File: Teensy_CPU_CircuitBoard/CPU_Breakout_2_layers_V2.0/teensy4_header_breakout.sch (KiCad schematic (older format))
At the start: 0 parts

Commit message: Start of V3 STM32
Imported symbols/footprints ...
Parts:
- added D9: D_RPP_Input_PMEG4010EGWX, Teensy_Footprint_Library:D_RPP_PMEG4010EGWX, symbol teensy4_header_breakout-cache:D_RPP_Input_PMEG4010EGWX
- added PS1: TEL_5-1211, Teensy_Footprint_Library:TEL51211, symbol teensy4_header_breakout-cache:TEL_5-1211
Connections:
- new net: PS1.2 (-VIN_(GND)_1), PS1.3 (-VIN_(GND)_2)
- new net: D9.1 (K), PS1.22 (+VIN_(VCC)_1), PS1.23 (+VIN_(VCC)_2)
- new net 12V_IN: D9.2 (A)
- new net Ground: PS1.16 (-VOUT)
- new net Vinn_5V: PS1.14 (+VOUT)
- no-connect marks 0 -> 1
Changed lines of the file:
@@
 $Descr A4 11693 8268
 encoding utf-8
-Sheet 1 6
+Sheet 1 5
 Title ""
 Date ""
@@
 $EndDescr
 $Sheet
-S 2400 4200 950  1150
+S 1650 4650 950  1150
 U 5DE81E30
 F0 "LM324" 50
@@
 $EndSheet
 $Sheet
-S 2300 1200 1200 1200
+S 1500 1150 1200 1200
 U 5DE8C472
 F0 "MCP2551" 50
@@
 $EndSheet
 $Sheet
-S 4500 1000 1100 1600
+S 3700 950  1100 1600
 U 5DE8C4DF
 F0 "microSD" 50
@@
 $EndSheet
 $Sheet
-S 6650 950  1000 1750
-U 5DE8C550
-F0 "VoltageReg" 50
-F1 "NCV890430MW50TXG.sch" 50
-$EndSheet
-$Sheet
-S 6700 3650 1050 1900
+S 3750 4200 1050 1900
 U 5DE8C5CE
 F0 "T4" 50
 F1 "Teensy4.0.sch" 50
 $EndSheet
+Text GLabel 9550 1650 2    50   Input ~ 0
+12V_IN
+Text GLabel 9250 1950 2    50   Input ~ 0
+Vinn_5V
+Text GLabel 6700 1650 0    50   Input ~ 0
+12V_Ground
+$Comp
+L teensy4_header_breakout-cache:TEL_5-1211 PS1
+U 1 1 5FAC174D
+P 7350 1650
+F 0 "PS1" H 8300 1915 50  0000 C CNN
+F 1 "TEL_5-1211" H 8300 1824 50  0000 C CNN
+F 2 "Teensy_Footprint_Library:TEL51211" H 9100 1750 50  0001 L CNN
+F 3 "https://www.tracopower.com/products/tel5.pdf" H 9100 1650 50  0001 L CNN
+F 4 "TEL5 DC-DC converter,9-18Vin 5V 5W TRACOPOWER Isolated DC-DC Converter, Vin 9  18 V dc, Vout 5V dc, I/O isolation 1500V dc" H 9100 1550 50  0001 L CNN "Description"
+F 5 "10.45" H 9100 1450 50  0001 L CNN "Height"
+F 6 "Traco Power" H 9100 1350 50  0001 L CNN "Manufacturer_Name"
+F 7 "TEL 5-1211" H 9100 1250 50  0001 L CNN "Manufacturer_Part_Number"
+F 8 "495-TEL-5-1211" H 9100 950 50  0001 L CNN "Mouser Part Number"
+F 9 "https://www.mouser.co.uk/ProductDetail/TRACO-Power/TEL-5-1211?qs=ckJk83FOD0WBOuRLitdGqQ%3D%3D" H 9100 850 50  0001 L CNN "Mouser Price/Stock"
+	1    7350 1650
+	1    0    0    -1
+$EndComp
+NoConn ~ 7350 1850
+Text GLabel 9250 1850 2    50   Input ~ 0
+Ground
+Wire Wire Line
+	9250 1750 9250 1650
+Wire Wire Line
+	7350 1650 7350 1750
+$Comp
+L teensy4_header_breakout-cache:D_RPP_Input_PMEG4010EGWX D9
+U 1 1 5FACD4C4
+P 9400 1650
+F 0 "D9" H 9400 1867 50  0000 C CNN
+F 1 "D_RPP_Input_PMEG4010EGWX" H 9400 1776 50  0000 C CNN
+F 2 "Teensy_Footprint_Library:D_RPP_PMEG4010EGWX" H 9400 1650 50  0001 C CNN
+F 3 "~" H 9400 1650 50  0001 C CNN
+	1    9400 1650
+	1    0    0    -1
+$EndComp
+Connection ~ 9250 1650
 $EndSCHEMATC

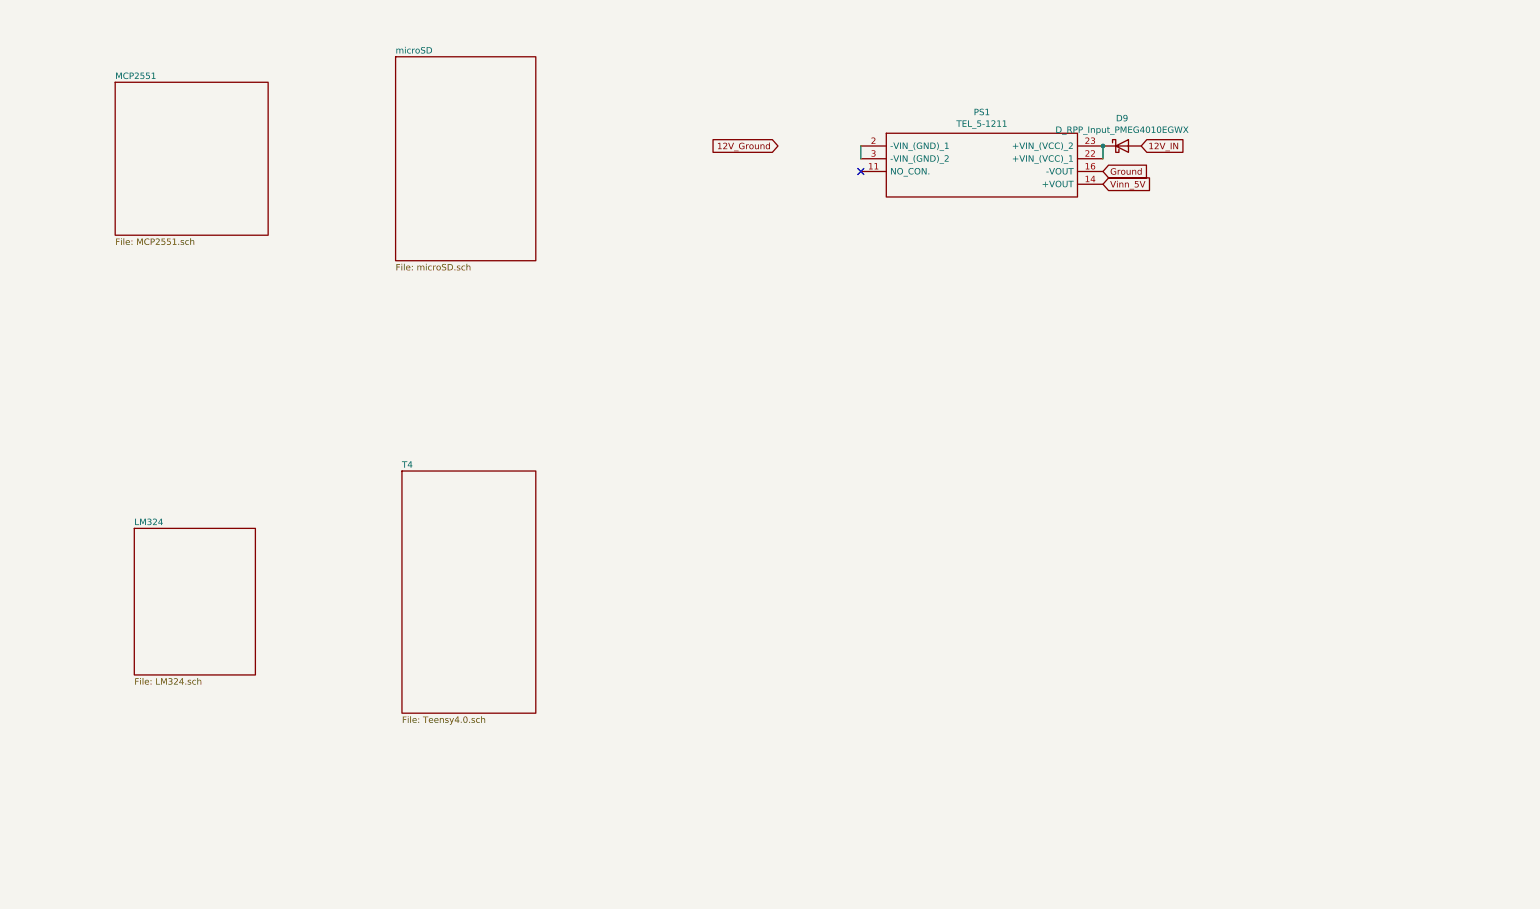
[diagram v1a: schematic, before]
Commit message: Suspension disp senson schematic done
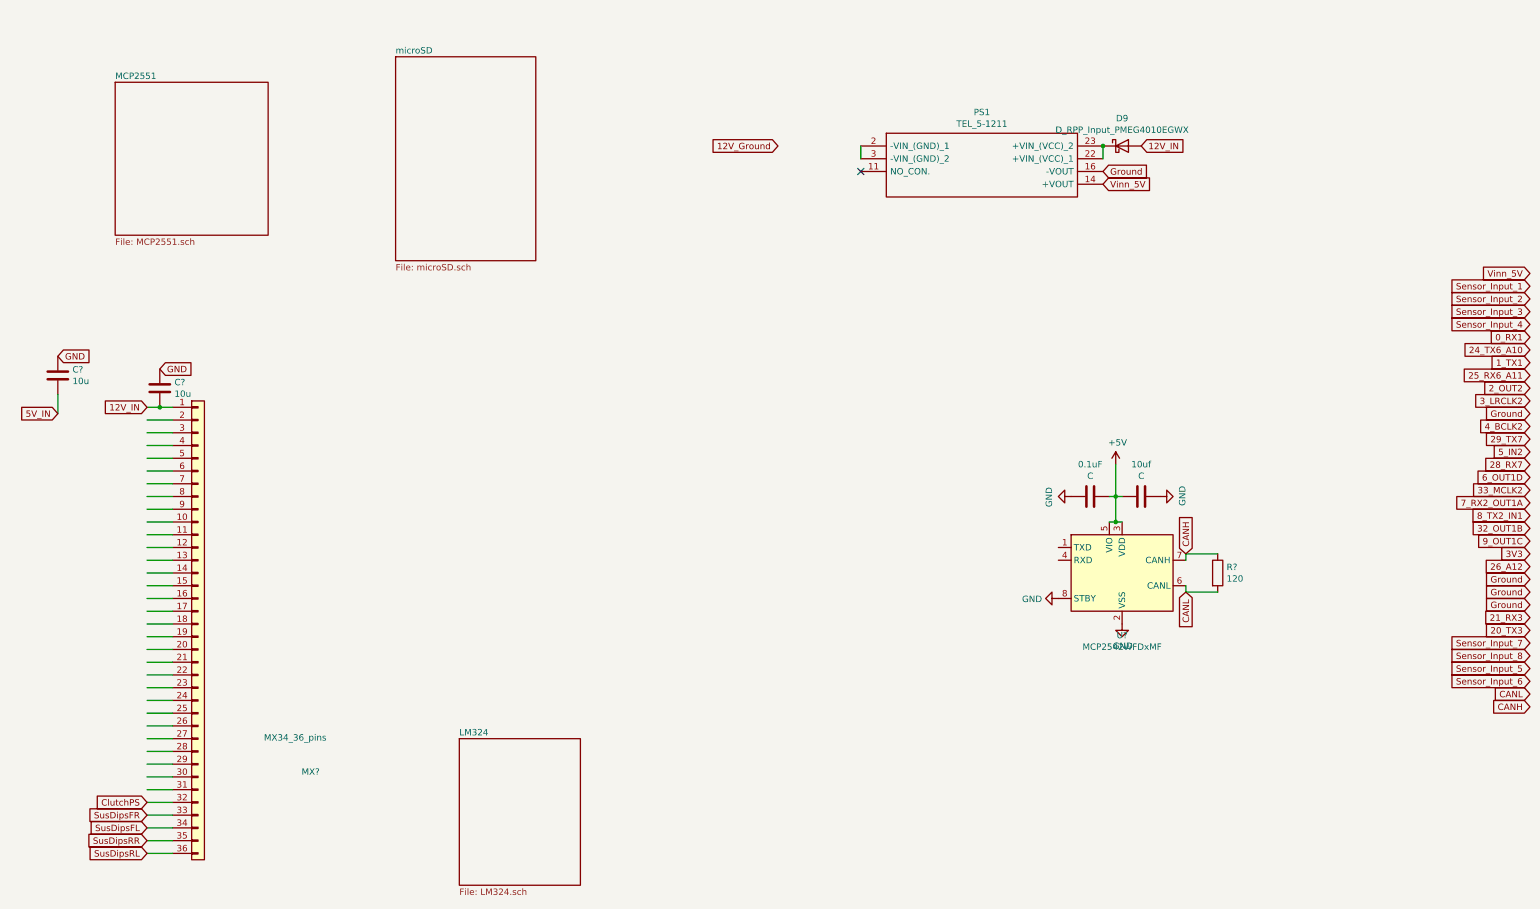
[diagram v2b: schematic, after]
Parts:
- added 0.1uF, 10uf: C, symbol Device:C
- added C? (x2): 10u, Capacitor_SMD:C_0603_1608Metric, symbol Device:C
- added MX?: MX34_36_pins, Teensy_Footprint_Library:Connector_MX34_36pins, symbol teensy4_header_breakout-cache:MX34_36_pins
- added R?: 120, symbol Device:R
- added U?: MCP2542WFDxMF, Package_DFN_QFN:DFN-8-1EP_3x3mm_P0.65mm_EP1.55x2.4mm, symbol Interface_CAN_LIN:MCP2542WFDxMF
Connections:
- net labels added: +5V, 0_RX1, 1_TX1, 20_TX3, 21_RX3, 24_TX6_A10, 25_RX6_A11, 26_A12, 28_RX7, 29_TX7, 2_OUT2, 32_OUT1B, 33_MCLK2, 3V3, 3_LRCLK2, 4_BCLK2, 5V_IN, 5_IN2, 6_OUT1D, 7_RX2_OUT1A, 8_TX2_IN1, 9_OUT1C, CANH, CANL, ClutchPS, GND, Sensor_Input_1, Sensor_Input_2, Sensor_Input_3, Sensor_Input_4, Sensor_Input_5, Sensor_Input_6, Sensor_Input_7, Sensor_Input_8, SusDipsFL, SusDipsFR, SusDipsRL, SusDipsRR
- wire segments 2 -> 50

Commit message: Added footprints diodes ++
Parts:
- added 10uF?, 10uf?: C, Capacitor_SMD:C_0603_1608Metric, symbol Device:C
- added C8: 10u, Capacitor_SMD:C_0603_1608Metric_Pad1.05x0.95mm_HandSolder, symbol Device:C
- added D5: D_Schottky, symbol Device:D_Schottky
- added F1: Polyfuse_Small, symbol Device:Polyfuse_Small
- added R?: 120, symbol Device:R
- added SDcard1: Micro_SD_Card, Teensy_Footprint_Library:Molex_502774-0891, symbol Connector:Micro_SD_Card
- added U?: MCP2542WFDxMF, Package_DFN_QFN:DFN-8-1EP_3x3mm_P0.65mm_EP1.55x2.4mm, symbol Interface_CAN_LIN:MCP2542WFDxMF
- 10uF1: renamed from 0.1uF; footprint (none) -> Capacitor_SMD:C_0603_1608Metric
- 10uf1: renamed from 10uf; footprint (none) -> Capacitor_SMD:C_0603_1608Metric
- gave numbers to parts that had none: 5
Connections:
- net labels added: +3.3V, 3.3V, CS_SD, MISO_SD, MOSI_SD, SD_SCK
- wire segments 50 -> 65
- no-connect marks 1 -> 3
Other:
- moved on the sheet: 10uF1, 10uf1, D9, PS1, R7, U1
